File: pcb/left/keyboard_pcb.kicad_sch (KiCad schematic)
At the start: 33 parts, among them J1 TRRS, K00 KEYSW, K01 KEYSW, K02 KEYSW, K03 KEYSW, K04 KEYSW, K05 KEYSW, K10 KEYSW, K11 KEYSW, K12 KEYSW, K13 KEYSW, K14 KEYSW, K15 KEYSW, K20 KEYSW, K21 KEYSW, K22 KEYSW, K23 KEYSW, K24 KEYSW, K25 KEYSW, K30 KEYSW, K31 KEYSW, K32 KEYSW, U2 Pico

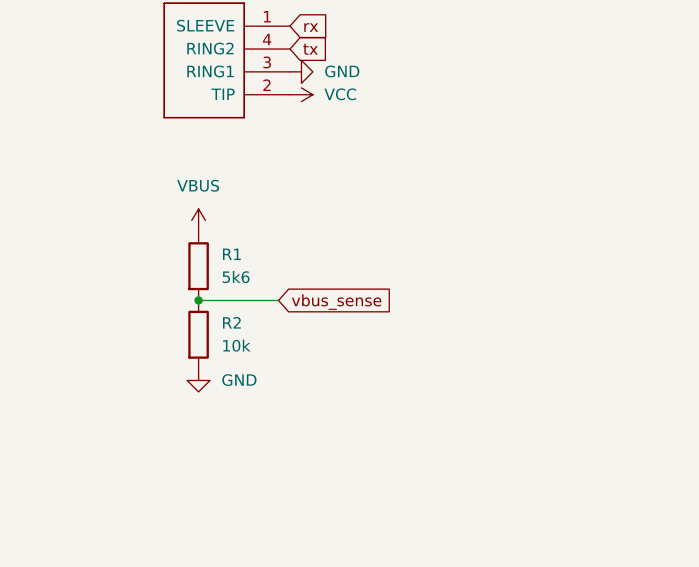
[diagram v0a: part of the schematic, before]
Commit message: Remove VBUS sense
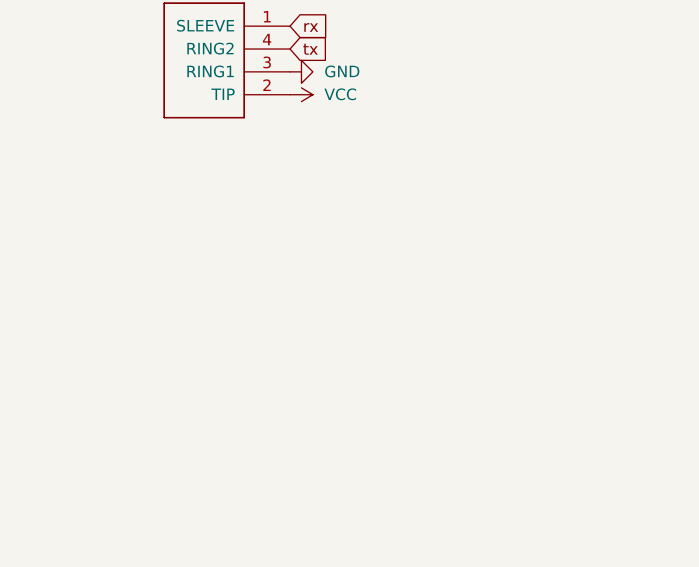
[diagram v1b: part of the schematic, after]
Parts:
- removed R1: 5k6, Resistor_SMD:R_1206_3216Metric_Pad1.30x1.75mm_HandSolder, symbol Device:R
- removed R2: 10k, Resistor_SMD:R_1206_3216Metric_Pad1.30x1.75mm_HandSolder, symbol Device:R
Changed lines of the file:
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@@
     (rev "rev1.0")
-  )
-  (junction (at 44.45 134.62) (diameter 0) (color 0 0 0 0)
   )
   (no_connect (at 68.58 49.53))
@@
     (stroke (width 0) (type default))
   )
-  (wire (pts (xy 44.45 134.62) (xy 53.34 134.62))
-    (stroke (width 0) (type default))
-  )
   (wire (pts (xy 68.58 77.47) (xy 73.66 77.47))
     (stroke (width 0) (type default))
@@
     )
   )
-  (global_label "vbus_sense" (shape input) (at 53.34 134.62 0) (fields_autoplaced)
-    (effects (font (size 1.27 1.27)) (justify left))
-    (property "Intersheetrefs" "${INTERSHEET_REFS}" (at 66.3969 134.5406 0)
-      (effects (font (size 1.27 1.27)) (justify left) hide)
-    )
-  )
   (global_label "tx" (shape input) (at 54.61 106.68 0) (fields_autoplaced)
     (effects (font (size 1.27 1.27)) (justify left))
@@
     )
   )
-  (symbol (lib_id "power:VBUS") (at 44.45 127 0) (unit 1)
-    (in_bom yes) (on_board yes) (dnp no) (fields_autoplaced)
-    (property "Reference" "#PWR0125" (at 44.45 130.81 0)
-      (effects (font (size 1.27 1.27)) hide)
-    )
-    (property "Value" "VBUS" (at 44.45 121.92 0)
-      (effects (font (size 1.27 1.27)))
-    )
-    (property "Footprint" "" (at 44.45 127 0)
-      (effects (font (size 1.27 1.27)) hide)
-    )
-    (property "Datasheet" "" (at 44.45 127 0)
-      (effects (font (size 1.27 1.27)) hide)
-    )
-    (pin "1")
-    (instances
-      (project "keyboard_pcb"
-        (path "/9538e4ed-27e6-4c37-b989-9859dc0d49e8"
-          (reference "#PWR0125") (unit 1)
-        )
-      )
-    )
-  )
   (symbol (lib_id "keyboard_parts:KEYSW") (at 264.16 45.72 0) (mirror y) (unit 1)
     (in_bom yes) (on_board yes) (dnp no) (fields_autoplaced)
@@
         (path "/9538e4ed-27e6-4c37-b989-9859dc0d49e8"
           (reference "#PWR0135") (unit 1)
-        )
-      )
-    )
-  )
-  (symbol (lib_id "Device:R") (at 44.45 138.43 0) (unit 1)
-    (in_bom yes) (on_board yes) (dnp no) (fields_autoplaced)
-    (property "Reference" "R2" (at 46.99 137.1599 0)
-      (effects (font (size 1.27 1.27)) (justify left))
-    )
-    (property "Value" "10k" (at 46.99 139.6999 0)
-      (effects (font (size 1.27 1.27)) (justify left))
-    )
-    (property "Footprint" "Resistor_SMD:R_1206_3216Metric_Pad1.30x1.75mm_HandSolder" (at 42.672 138.43 90)
-      (effects (font (size 1.27 1.27)) hide)
-    )
-    (property "Datasheet" "~" (at 44.45 138.43 0)
-      (effects (font (size 1.27 1.27)) hide)
-    )
-    (pin "1")
-    (pin "2")
-    (instances
-      (project "keyboard_pcb"
-        (path "/9538e4ed-27e6-4c37-b989-9859dc0d49e8"
-          (reference "R2") (unit 1)
         )
       )
@@
     )
   )
-  (symbol (lib_id "power:GND") (at 44.45 142.24 0) (unit 1)
-    (in_bom yes) (on_board yes) (dnp no) (fields_autoplaced)
-    (property "Reference" "#PWR0127" (at 44.45 148.59 0)
-      (effects (font (size 1.27 1.27)) hide)
-    )
-    (property "Value" "GND" (at 46.99 143.5099 0)
-      (effects (font (size 1.27 1.27)) (justify left))
-    )
-    (property "Footprint" "" (at 44.45 142.24 0)
-      (effects (font (size 1.27 1.27)) hide)
-    )
-    (property "Datasheet" "" (at 44.45 142.24 0)
-      (effects (font (size 1.27 1.27)) hide)
-    )
-    (pin "1")
-    (instances
-      (project "keyboard_pcb"
-        (path "/9538e4ed-27e6-4c37-b989-9859dc0d49e8"
-          (reference "#PWR0127") (unit 1)
-        )
-      )
-    )
-  )
   (symbol (lib_id "power:VCC") (at 68.58 31.75 270) (unit 1)
     (in_bom yes) (on_board yes) (dnp no) (fields_autoplaced)
@@
         )
       )
-    )
-  )
-  (symbol (lib_id "Device:R") (at 44.45 130.81 0) (unit 1)
-    (in_bom yes) (on_board yes) (dnp no) (fields_autoplaced)
-    (property "Reference" "R1" (at 46.99 129.5399 0)
-      (effects (font (size 1.27 1.27)) (justify left))
-    )
-    (property "Value" "5k6" (at 46.99 132.0799 0)
-      (effects (font (size 1.27 1.27)) (justify left))
-    )
-    (property "Footprint" "Resistor_SMD:R_1206_3216Metric_Pad1.30x1.75mm_HandSolder" (at 42.672 130.81 90)
-      (effects (font (size 1.27 1.27)) hide)
-    )
-    (property "Datasheet" "~" (at 44.45 130.81 0)
-      (effects (font (size 1.27 1.27)) hide)
-    )
-    (pin "1")
-    (pin "2")
-    (instances
-      (project "keyboard_pcb"
-        (path "/9538e4ed-27e6-4c37-b989-9859dc0d49e8"
-          (reference "R1") (unit 1)
-        )
-      )

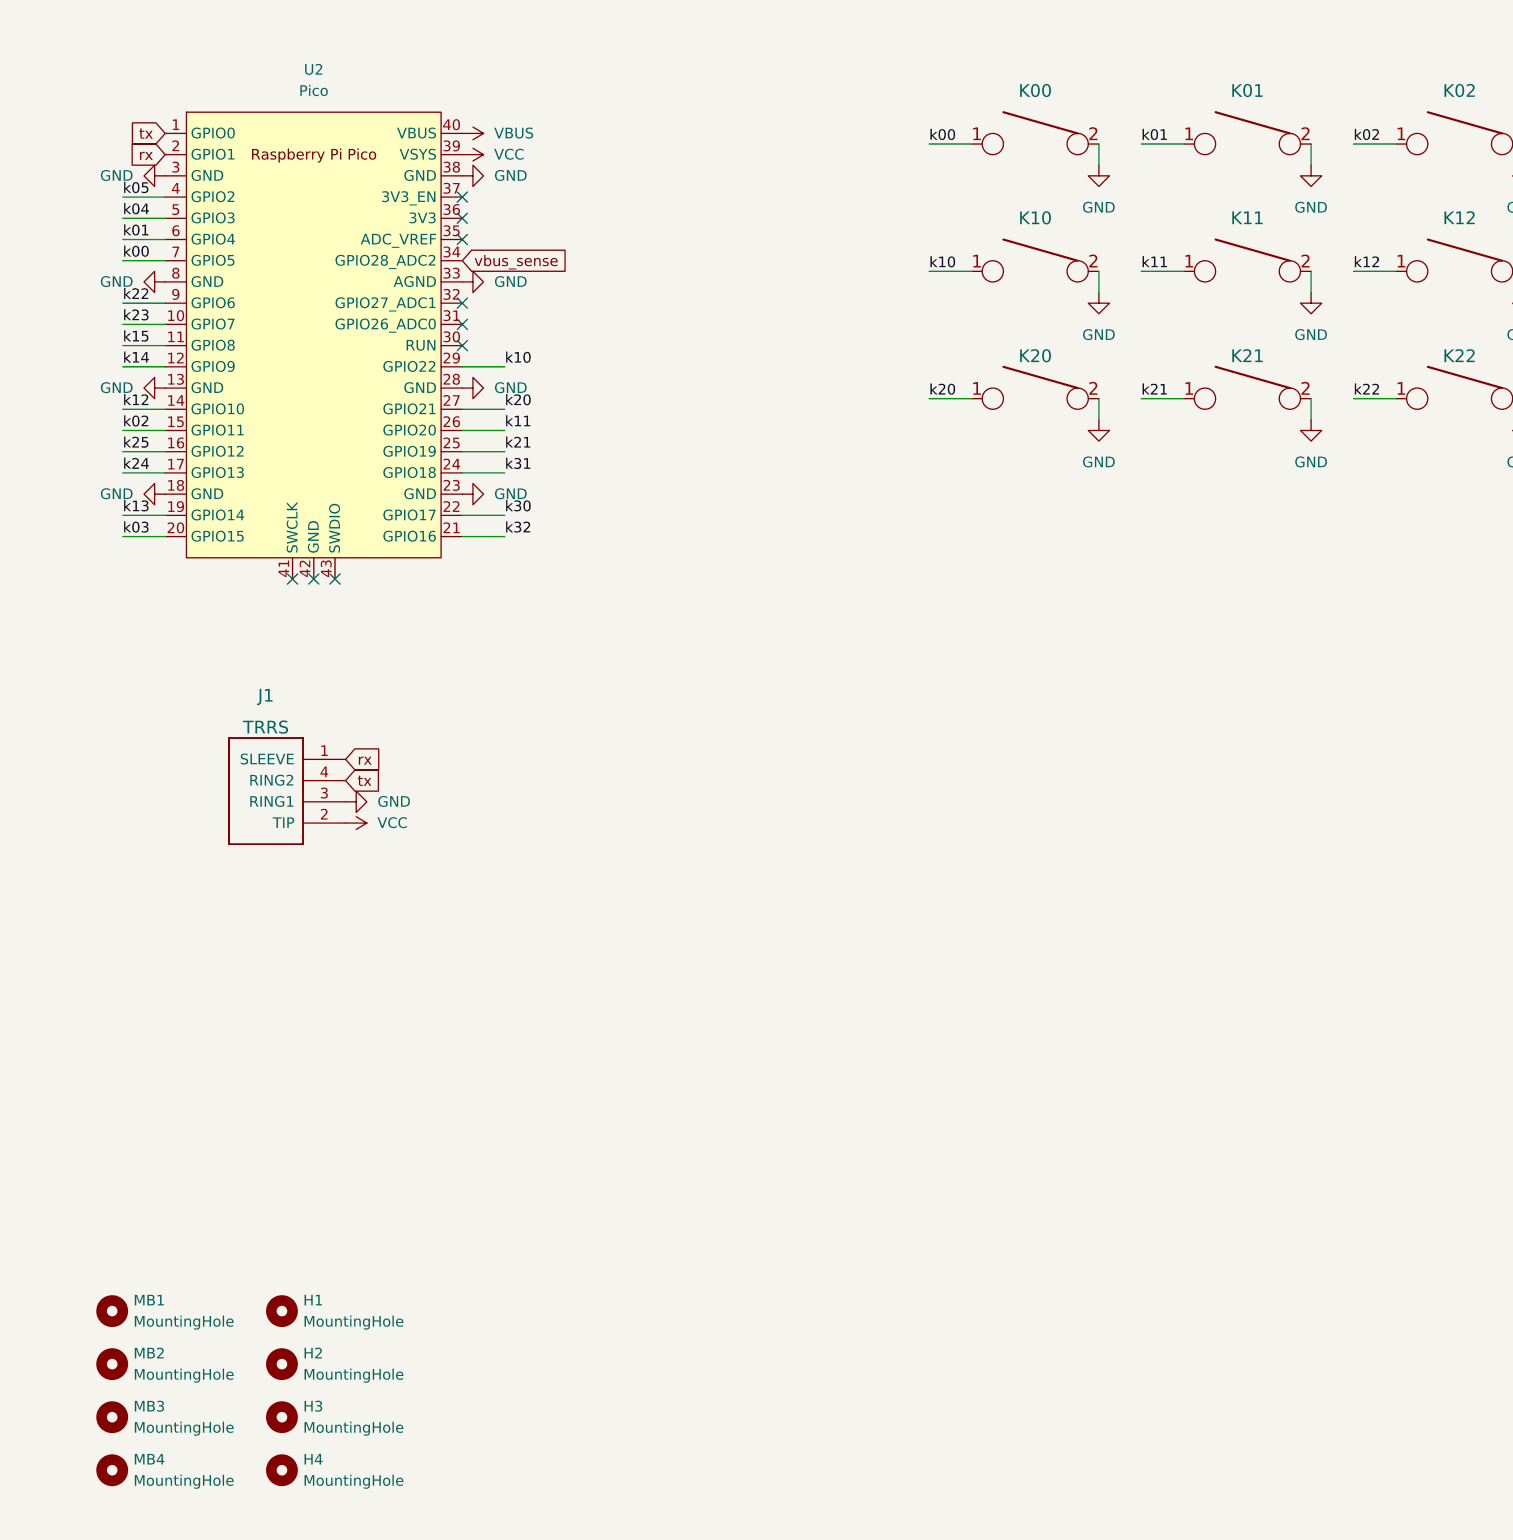
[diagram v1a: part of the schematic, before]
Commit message: Updated schematic
 * Replace Pico with Pro Micro
 * Copy ProMicro footprint from [marbastlib](https://github.com/ebastler/marbastlib) and update with flipped pin labels
 * Add battery connections
 * Add RGB LED
 * Add reset switch
 * Switch split keyboard connection from audio jack to USB C
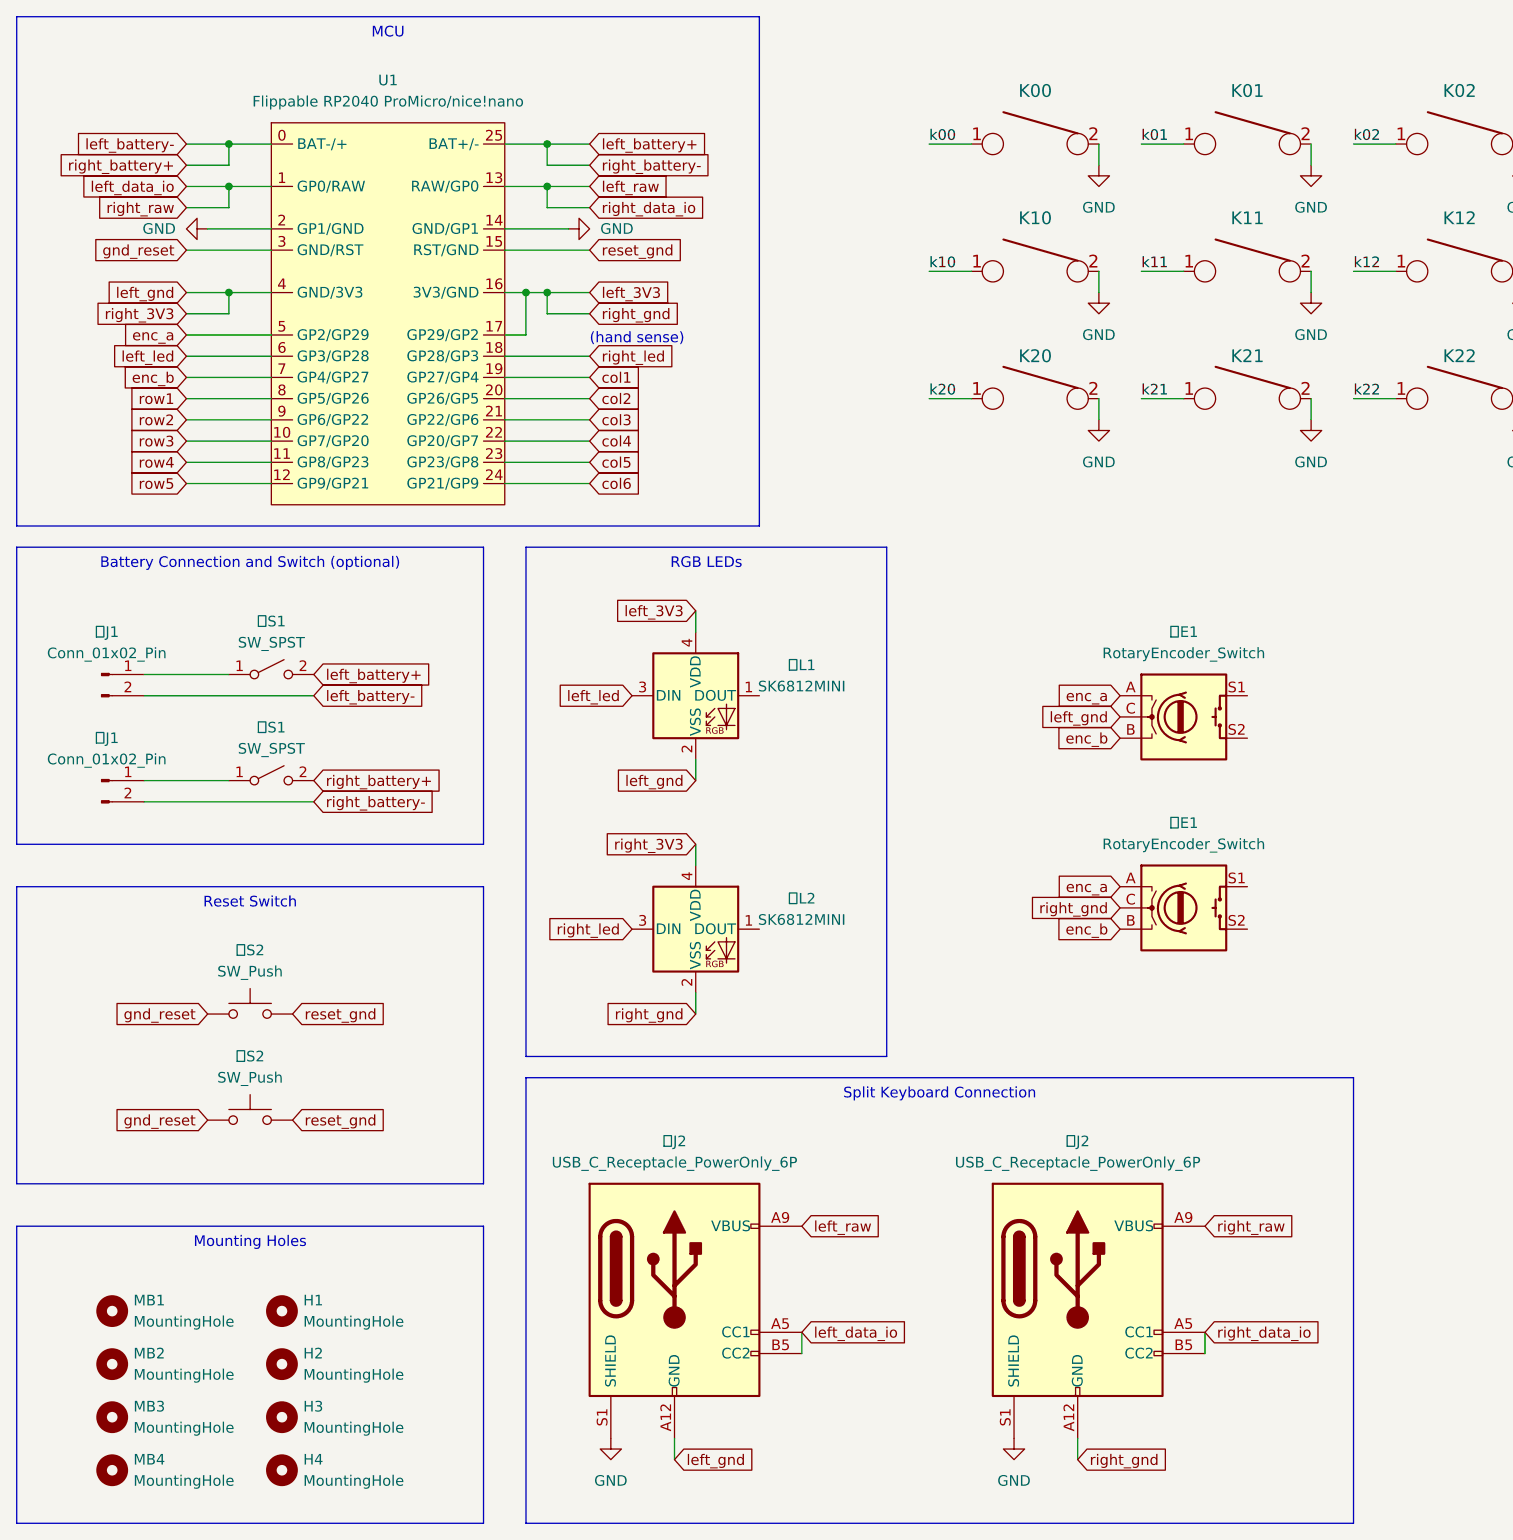
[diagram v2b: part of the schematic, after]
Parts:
- removed J1: TRRS, Resistor_SMD:R_1206_3216Metric_Pad1.30x1.75mm_HandSolder, symbol keebio:TRRS
- removed U2: Pico, RPi_Pico:RPi_Pico_SMD_TH, symbol KiCad-RP-Pico:Pico
- added U1: Flippable RP2040 ProMicro/nice!nano, PCM_marbastlib-xp-promicroish:ProMicro_USBup, symbol _Project Library:ProMicro_Flippable
- added 右E1, 左E1: RotaryEncoder_Switch, symbol Device:RotaryEncoder_Switch
- added 右J1, 左J1: Conn_01x02_Pin, symbol Connector:Conn_01x02_Pin
- added 右J2, 左J2: USB_C_Receptacle_PowerOnly_6P, symbol Connector:USB_C_Receptacle_PowerOnly_6P
- added 右L2, 左L1: SK6812MINI, LED_SMD:LED_SK6812MINI_PLCC4_3.5x3.5mm_P1.75mm, symbol LED:SK6812MINI
- added 右S1, 左S1: SW_SPST, symbol Switch:SW_SPST
- added 右S2, 左S2: SW_Push, symbol Switch:SW_Push
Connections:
- net GND: now also U1.14 (GND/GP1), U1.2 (GP1/GND), 右J2.S1 (SHIELD), 左J2.S1 (SHIELD)
- new net: 左J1.1 (Pin_1), 左S1.1 (A)
- new net: 右J1.1 (Pin_1), 右S1.1 (A)
- new net col1: U1.19 (GP27/GP4)
- new net col2: U1.20 (GP26/GP5)
- new net col3: U1.21 (GP22/GP6)
- new net col4: U1.22 (GP20/GP7)
- new net col5: U1.23 (GP23/GP8)
- new net col6: U1.24 (GP21/GP9)
- new net enc_a: U1.5 (GP2/GP29), 右E1.A, 左E1.A
- new net enc_b: U1.7 (GP4/GP27), 右E1.B, 左E1.B
- new net gnd_reset: U1.3 (GND/RST), 右S2.1, 左S2.1
- new net left_3V3: U1.16 (3V3/GND), U1.17 (GP29/GP2), 右E1.C, 右J2.A12 (GND), 右J2.B12 (GND), 右L2.2 (VSS), 左L1.4 (VDD)
- new net left_battery+: U1.25 (BAT+/-), 右J1.2 (Pin_2), 左S1.2 (B)
- new net left_battery-: U1.0 (BAT-/+), 右S1.2 (B), 左J1.2 (Pin_2)
- new net left_data_io: U1.1 (GP0/RAW), 右J2.A9 (VBUS), 右J2.B9 (VBUS), 左J2.A5 (CC1), 左J2.B5 (CC2)
- new net left_gnd: U1.4 (GND/3V3), 右L2.4 (VDD), 左E1.C, 左J2.A12 (GND), 左J2.B12 (GND), 左L1.2 (VSS)
- new net left_led: U1.6 (GP3/GP28), 左L1.3 (DIN)
- new net left_raw: U1.13 (RAW/GP0), 右J2.A5 (CC1), 右J2.B5 (CC2), 左J2.A9 (VBUS), 左J2.B9 (VBUS)
- new net reset_gnd: U1.15 (RST/GND), 右S2.2, 左S2.2
- new net right_led: U1.18 (GP28/GP3), 右L2.3 (DIN)
- new net row1: U1.8 (GP5/GP26)
- new net row2: U1.9 (GP6/GP22)
- new net row3: U1.10 (GP7/GP20)
- new net row4: U1.11 (GP8/GP23)
- new net row5: U1.12 (GP9/GP21)
- no-connect marks 9 -> 0
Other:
- note added: "(hand sense)"
